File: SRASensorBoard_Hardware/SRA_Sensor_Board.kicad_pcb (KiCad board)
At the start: 2 copper layers, 124.5 x 81.3 mm, 80 parts, among them J1 USB_A, Q1 BSS138, Q2 BSS138, Q3 BSS138, Q4 BSS138, Q5 Q_PMOS_GDS, Q6 Q_NMOS_GSD, U1 FT230XS, U2 OKI, U3 OKI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

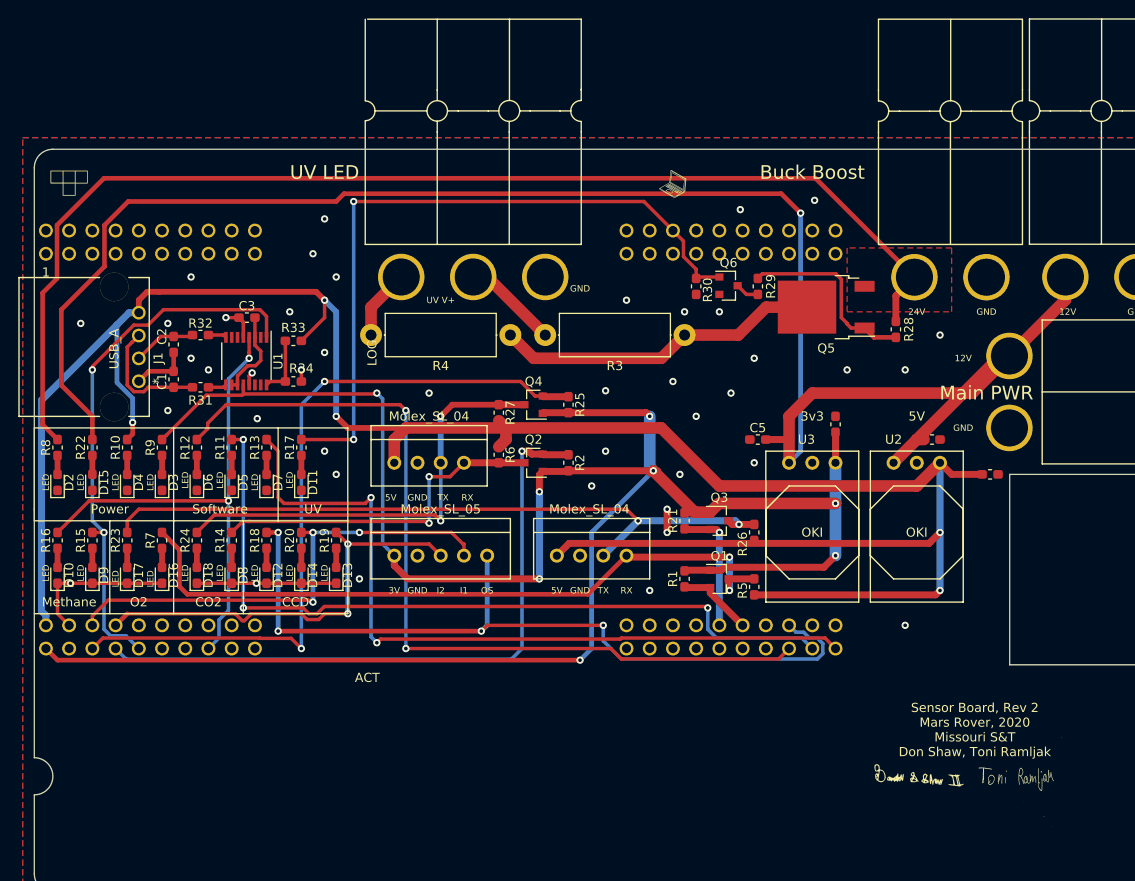
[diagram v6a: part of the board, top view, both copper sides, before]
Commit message: Rev 2 prt 2 changes
Updated UV led to current format
Removed CCD
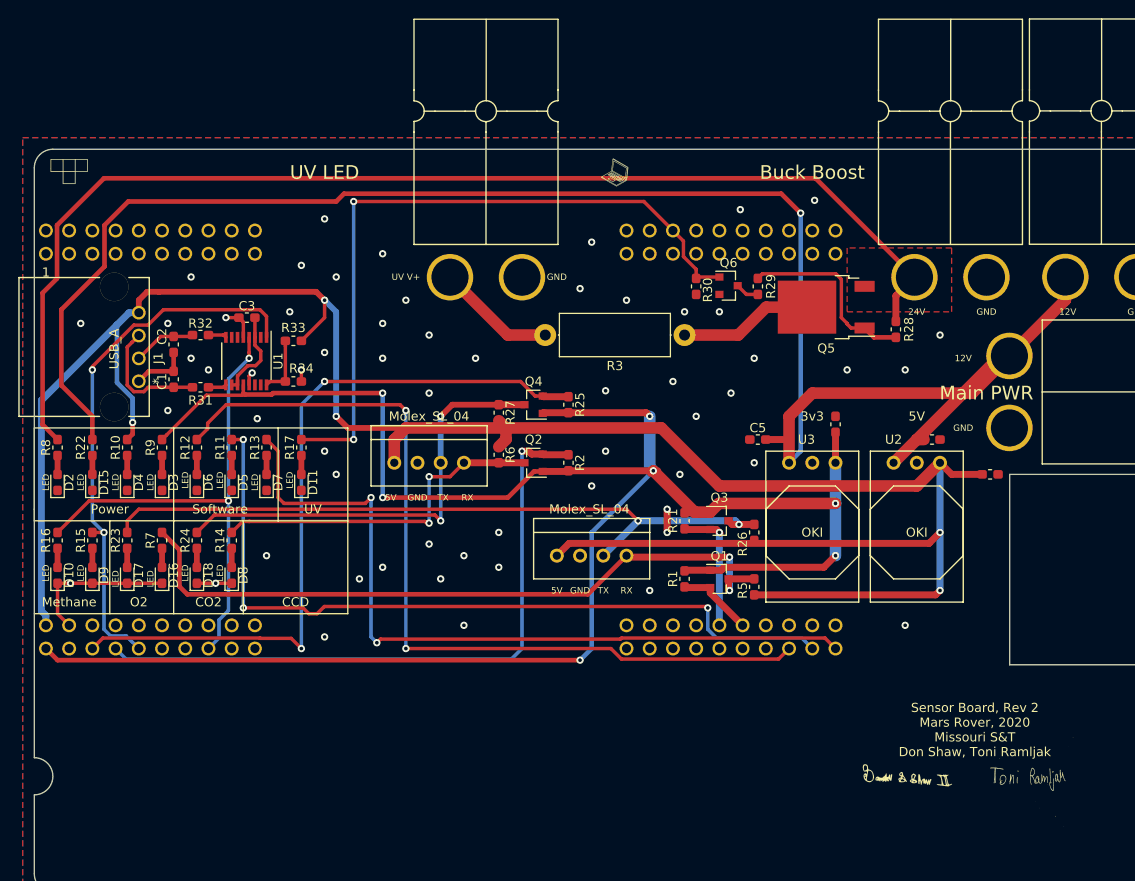
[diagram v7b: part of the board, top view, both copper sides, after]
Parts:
- removed Conn4: Molex_SL_05, MRDT_Connectors:MOLEX_SL_05_Vertical
- removed D12, D13, D14: LED, Diode_SMD:D_0603_1608Metric_Pad1.05x0.95mm_HandSolder
- removed R18, R19, R20: 330, Resistor_SMD:R_0603_1608Metric_Pad1.05x0.95mm_HandSolder
- removed R4: 4, Resistor_THT:R_Axial_DIN0414_L11.9mm_D4.5mm_P15.24mm_Horizontal
- Conn7: footprint MRDT_Connectors:Anderson_3_Horizontal_Side_by_Side -> MRDT_Connectors:Anderson_2_Horizontal_Side_by_Side
- R3: value 4 -> 2
- moved Conn7 17.5 mm to (121.9, 62.2)
- moved G*** 6.48 mm to (132.1, 50.8)
- moved G*** 1.27 mm to (177.8, 116.8)
- moved G*** 1.27 mm to (72.4, 50.8)
- moved G*** 1.27 mm to (163.8, 116.8)
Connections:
- U4 pad PE0: CCD_INT1 -> Net-(U4-PadPE0)
- U4 pad PE1: CCD_INT2 -> Net-(U4-PadPE1)
- U4 pad PK3: CCD_OS -> Net-(U4-PadPK3)
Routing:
- net CCD_OS: track 88.8 -> 0.00 mm, vias 4 -> 0
- net CCD_INT1: track 53.1 -> 0.00 mm, vias 3 -> 0
- net CCD_INT2: track 47.3 -> 0.00 mm, vias 2 -> 0
- net Net-(Q5-Pad2): track 35.8 -> 14.7 mm
- net +3V3: track 244.9 -> 227.7 mm, vias 8 -> 7
- net GND: track 47.2 -> 35.7 mm, vias 42 -> 56
- net Net-(Conn7-Pad3): track 7.72 -> 0.00 mm
- net Net-(Conn7-Pad2): track 10.5 -> 13.0 mm
- net Net-(D14-Pad2): track 2.06 -> 0.00 mm
- net Net-(D13-Pad2): track 2.06 -> 0.00 mm
- net Net-(D12-Pad2): track 2.06 -> 0.00 mm
- net (no net): vias 0 -> 3
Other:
- board text removed: "3V"
- board text removed: "I1"
- board text removed: "I2"
- board text removed: "OS"
